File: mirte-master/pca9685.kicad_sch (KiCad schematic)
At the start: 1 part, among them J9 pca9685

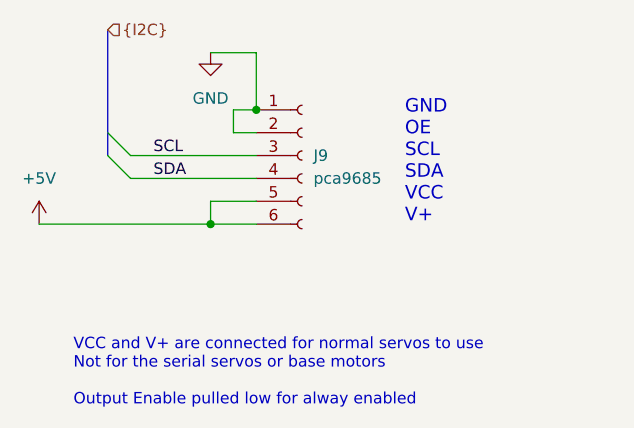
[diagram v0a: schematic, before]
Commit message: mirte-master schematic cleanup and readabilityimprovements
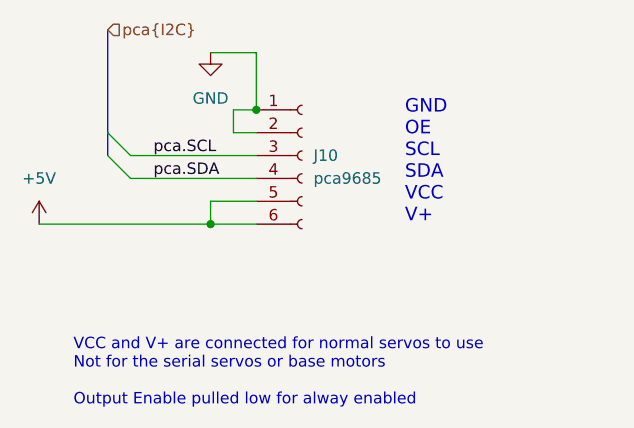
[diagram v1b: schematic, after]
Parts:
- renumbered J9 to J10
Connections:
- net SCL renamed pca.SCL
- net SDA renamed pca.SDA
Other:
- title: (none) -> ${PROJECTNAME}
